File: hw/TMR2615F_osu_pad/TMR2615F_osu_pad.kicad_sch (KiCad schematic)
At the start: 78 parts, among them J1 TYPE-C-31-M-12, J10 Conn_01x04, J2 TYPE-C-31-M-12, J3 Conn_01x02, J4 TYPE-C-31-M-12, J5 XY-SH1_0-4A61, J7 Conn_01x10, J8 Conn_01x06, J9 Conn_01x23, SW1 SKSGPAE010, SW2 SKSGPAE010, U1 CA-IS3722CHS, U2 SRV05-4A, U28 SRV05-4A, U3 TMUX1574RSVR, U4 LM66100DCK, U5 AP22653W6-7, U6 SRV05-4A, U7 AT32F405RBT7-7, U8 XC6206P332MR, U9 TPS7A4700, X1 X322512MSB4SI

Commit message: Update TMR2615F_osu_pad layout/schematic, bump library submodule, add ERC report
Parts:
- removed NT1: NetTie_2, NetTie:NetTie-2_SMD_Pad2.0mm, symbol Device:NetTie_2
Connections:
- net GNDA is gone; now on net GND: C26.2, C27.1, C31.1, C32.1, C33.1, C5.1, J8.1 (Pin_1), R10.2, U3.6 (GND), U7.12 (VSSA), U9.11 (0P2V), U9.12 (0P1V), U9.17 (NC), U9.18 (NC), U9.19 (NC), U9.2 (NC), U9.21 (TP), U9.7 (GND), U9.8 (1P6V)
- net +3.3V: now also R7.2
- net +5V: now also U5.3 (EN/EN#)
- net IO9: now also R7.1, U5.4 (FAULT#); no longer U5.3 (EN/EN#)
- net VBUS_B: no longer R7.2

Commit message: before foob
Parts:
- removed C1, C4, C5: CL05B104KB54PNC, Capacitor_SMD:C_0402_1005Metric, symbol Basic_Capacitors_Resistors__C:CL05B104KB54PNC
- removed C11, C12, C13, C14, C16, C17: CL21A226MAQNNNE, Capacitor_SMD:C_0805_2012Metric, symbol Basic_Capacitors_Resistors__C:CL21A226MAQNNNE
- removed J3: Conn_01x02, Connector_PinHeader_2.54mm:PinHeader_1x02_P2.54mm_Horizontal, symbol Connector_Generic:Conn_01x02
- removed R13, R14, R15, R16: 0402WGF0000TCE, Resistor_SMD:R_0402_1005Metric, symbol Basic_Capacitors_Resistors__C:0402WGF0000TCE
- removed R7: 0402WGF1002TCE, Resistor_SMD:R_0402_1005Metric, symbol Basic_Capacitors_Resistors__C:0402WGF1002TCE
- removed R8: 0402WGF3301TCE, Resistor_SMD:R_0402_1005Metric, symbol Basic_Capacitors_Resistors__C:0402WGF3301TCE
- removed U1: CA-IS3722CHS, Isolator__C:SOIC-8_L4.9-W3.9-P1.27-LS6.0-BL, symbol Isolator__C:CA-IS3722CHS
- added C1, C2, C3, C4, C5, C6: CL21A226MAQNNNE, Capacitor_SMD:C_0805_2012Metric, symbol Basic_Capacitors_Resistors__C:CL21A226MAQNNNE
- added C10: CL10B473KB8NNNC, Capacitor_SMD:C_0603_1608Metric, symbol Basic_Capacitors_Resistors__C:CL10B473KB8NNNC
- added C12: CL21A106KAYNNNE, Capacitor_SMD:C_0805_2012Metric, symbol Basic_Capacitors_Resistors__C:CL21A106KAYNNNE
- added C28, C29: CL05B104KB54PNC, Capacitor_SMD:C_0402_1005Metric, symbol Basic_Capacitors_Resistors__C:CL05B104KB54PNC
- added D1: 1N4148WS_T4, Diode_SMD:D_SOD-323_HandSoldering, symbol Diode__C:1N4148WS_T4
- added FID1, FID2, FID3: Fiducial, Fiducial:Fiducial_1mm_Mask2mm, symbol Mechanical:Fiducial
- added H1, H2, H3: MountingHole_Pad, MountingHole:MountingHole_2.2mm_M2_Pad_Via, symbol Mechanical:MountingHole_Pad
- added R1, R10, R2, R26, R4, R6, R9: 0402WGF1002TCE, Resistor_SMD:R_0402_1005Metric, symbol Basic_Capacitors_Resistors__C:0402WGF1002TCE
- added R12, R13: 0402WGF5101TCE, Resistor_SMD:R_0402_1005Metric, symbol Basic_Capacitors_Resistors__C:0402WGF5101TCE
- added R14, R27, R3, R7: 0402WGF1200TCE, Resistor_SMD:R_0402_1005Metric, symbol Basic_Capacitors_Resistors__C:0402WGF1200TCE
- added R8: 0402WGF3300TCE, Resistor_SMD:R_0402_1005Metric, symbol Basic_Capacitors_Resistors__C:0402WGF3300TCE
- added TP1, TP10, TP11, TP12, TP13, TP14, TP15, TP16, TP2, TP3, TP4, TP5, TP6, TP7, TP8, TP9: TestPoint, TestPoint:TestPoint_Pad_D1.0mm, symbol Connector:TestPoint
- added U1: SRV05-4A, Diode__C:SOT-23-6, symbol Diode__C:SRV05-4
- added U12: SK6812MINI-E, LED__C:LED-SMD_4P-L3.2-W2.8-LS5.9_SK6812MINI-E, symbol LED__C:SK6812MINI-E_C5149201
- added U7: LM66100DCK, Package_TO_SOT_SMD:SOT-363_SC-70-6, symbol Power_Management:LM66100DCK
- R17: renamed from R4; now fitted
- R18: renamed from R5; now fitted
- renumbered C10 to C11, C31 to C13, C32 to C14, C8 to C15, C9 to C16, C2 to C17, C3 to C18, C18 to C19, C19 to C20, C20 to C21, C26 to C22, C27 to C23, C21 to C24, C22 to C25, C23 to C26, C24 to C27, C15 to C30, C25 to C31, C30 to C32, C6 to C7, C7 to C8, C33 to C9, J4 to J2, J2 to J3, J5 to J4, J7 to J5, J9 to J6, J8 to J7, J10 to J8, J6 to J9, R6 to R11, R24 to R15, R26 to R16, R1 to R19, R2 to R20, R25 to R21, R23 to R22, R10 to R23, R11 to R24, R12 to R25, R9 to R28, R3 to R5, U7 to U10, U3 to U11, U4 to U2, U5 to U3, U9 to U4, U6 to U5, U2 to U6, U28 to U9
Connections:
- net IO8 is gone; now on net IO7: J6.23 (Pin_23), U10.4 (PC15)
- net +3.3V: now also J6.4 (Pin_4), R5.2, U9.5 (VP), R1.2, R14.2, R2.2, R6.2, TP12.1, U1.5 (VP); no longer J6.3 (Pin_3)
- net +3.3VA: now also C28.2, TP3.1; no longer U11.13 (EN#)
- net +5V: now also J6.3 (Pin_3), U2.3 (~{CE}), C1.2, C2.2, C3.2, C4.2, C5.2, C6.2, D1.2 (A), TP11.1, U7.3 (~{CE}), U7.6 (VOUT); no longer C7.1, C8.2, J2.A4B9 (VBUS), J2.B4A9 (VBUS), J3.A4B9 (VBUS), J3.B4A9 (VBUS), J6.2 (Pin_2), R5.2, U3.1 (IN), U3.3 (EN/EN#), U9.5 (VP)
- net ADC1_IN0: now also TP13.1
- net ADC1_IN1: now also TP14.1
- net ADC1_IN2: now also TP15.1
- net ADC1_IN3: now also TP16.1
- net BOOT: now also R26.2
- net DIN: now also U12.4 (DOUT); no longer U10.62 (PB9)
- net GND: now also J5.9 (Pin_9), J6.16 (Pin_16), J6.2 (Pin_2), U11.13 (EN#), C1.1, C10.1, C12.2, C2.1, C28.1, C29.1, C3.1, C4.1, C5.1, C6.1, H1.1, H2.1, H3.1, R10.1, R12.1, R13.1, R26.1, R9.1, TP9.1, U1.2 (VN), U12.1 (GND), U7.2 (GND), U7.5 (ST); no longer J6.15 (Pin_15), U2.3 (~{CE})
- net I2C1_SCL: now also U9.3 (IO2), U9.4 (IO3); no longer U9.1 (IO1), U9.6 (IO4)
- net I2C1_SDA: now also U9.1 (IO1), U9.6 (IO4); no longer U9.3 (IO2), U9.4 (IO3)
- net I2C2_SCL: now also J6.11 (Pin_11); no longer J6.10 (Pin_10)
- net I2C2_SDA: now also J6.10 (Pin_10); no longer J6.9 (Pin_9)
- net IO1: now also J6.17 (Pin_17); no longer J6.16 (Pin_16)
- net IO2: now also J6.18 (Pin_18); no longer J6.17 (Pin_17)
- net IO3: now also J6.19 (Pin_19); no longer J6.18 (Pin_18)
- net IO4: now also J6.20 (Pin_20); no longer J6.19 (Pin_19)
- net IO5: now also J6.21 (Pin_21); no longer J6.20 (Pin_20)
- net IO6: now also J6.22 (Pin_22), U10.3 (PC14); no longer J6.21 (Pin_21), U10.2 (PC13)
- net IO7: no longer J6.22 (Pin_22), U10.3 (PC14)
- net SPI3_CS: now also J6.12 (Pin_12); no longer J6.11 (Pin_11)
- net SPI3_MISO: now also J6.14 (Pin_14); no longer J6.13 (Pin_13)
- net SPI3_MOSI: now also J6.15 (Pin_15); no longer J6.14 (Pin_14)
- net SPI3_SCK: now also J6.13 (Pin_13); no longer J6.12 (Pin_12)
- net TMUX_S4A: now also R8.1, TP6.1; no longer J5.10 (Pin_10)
- net TMUX_S4B: now also J5.10 (Pin_10); no longer J5.9 (Pin_9)
- net UART7_RX: now also U10.37 (PC6), R2.1, R3.2, U1.1 (IO1), U1.6 (IO4)
- net UART7_TX: now also U10.38 (PC7), R1.1, R7.2, U1.3 (IO2), U1.4 (IO3)
- net UART8_RX: now also J6.6 (Pin_6); no longer J6.5 (Pin_5)
- net UART8_TX: now also J6.5 (Pin_5); no longer J6.4 (Pin_4)
- net USART1_CK: now also J6.9 (Pin_9); no longer J6.8 (Pin_8)
- net USART1_RX: now also J6.7 (Pin_7); no longer J6.6 (Pin_6)
- net USART1_TX: now also J6.8 (Pin_8); no longer J6.7 (Pin_7)
- net VBUS_B: now also C12.1, R4.2, TP4.1
- net at J1.A6 (DP1), J1.B6 (DP2): now also R7.1, TP1.1
- net at J1.A7 (DN1), J1.B7 (DN2): now also R3.1, TP2.1
- net at J1.A5 (CC1): now also R13.2
- net at J1.B5 (CC2): now also R12.2
- net at R15.2, R22.2: now also R14.1
- net IO10 renamed LM_ST
- net LM_ST: now also TP5.1
- net IO9 renamed AP_FAULT
- net AP_FAULT: now also R6.1, TP7.1
- new net: C10.2, R4.1, R8.2, R9.2
- new net: R27.1, U12.2 (DIN)
- new net: R27.2, U10.62 (PB9)
- new net: C29.2, D1.1 (K), U12.3 (VDD)
- new net PW_PSTRH: R10.2, TP8.1, U10.2 (PC13), U3.3 (EN/EN#)
- new net VBUS_HOST: C7.1, C8.2, J3.A4B9 (VBUS), J3.B4A9 (VBUS), TP10.1, U3.1 (IN), U7.1 (VIN)
- no-connect marks 6 -> 14
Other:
- note removed: "For End User Installation"
- moved on the sheet: C11, C15, C16, C17, C18, C19, C20, C21, C22, C23, C24, C25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

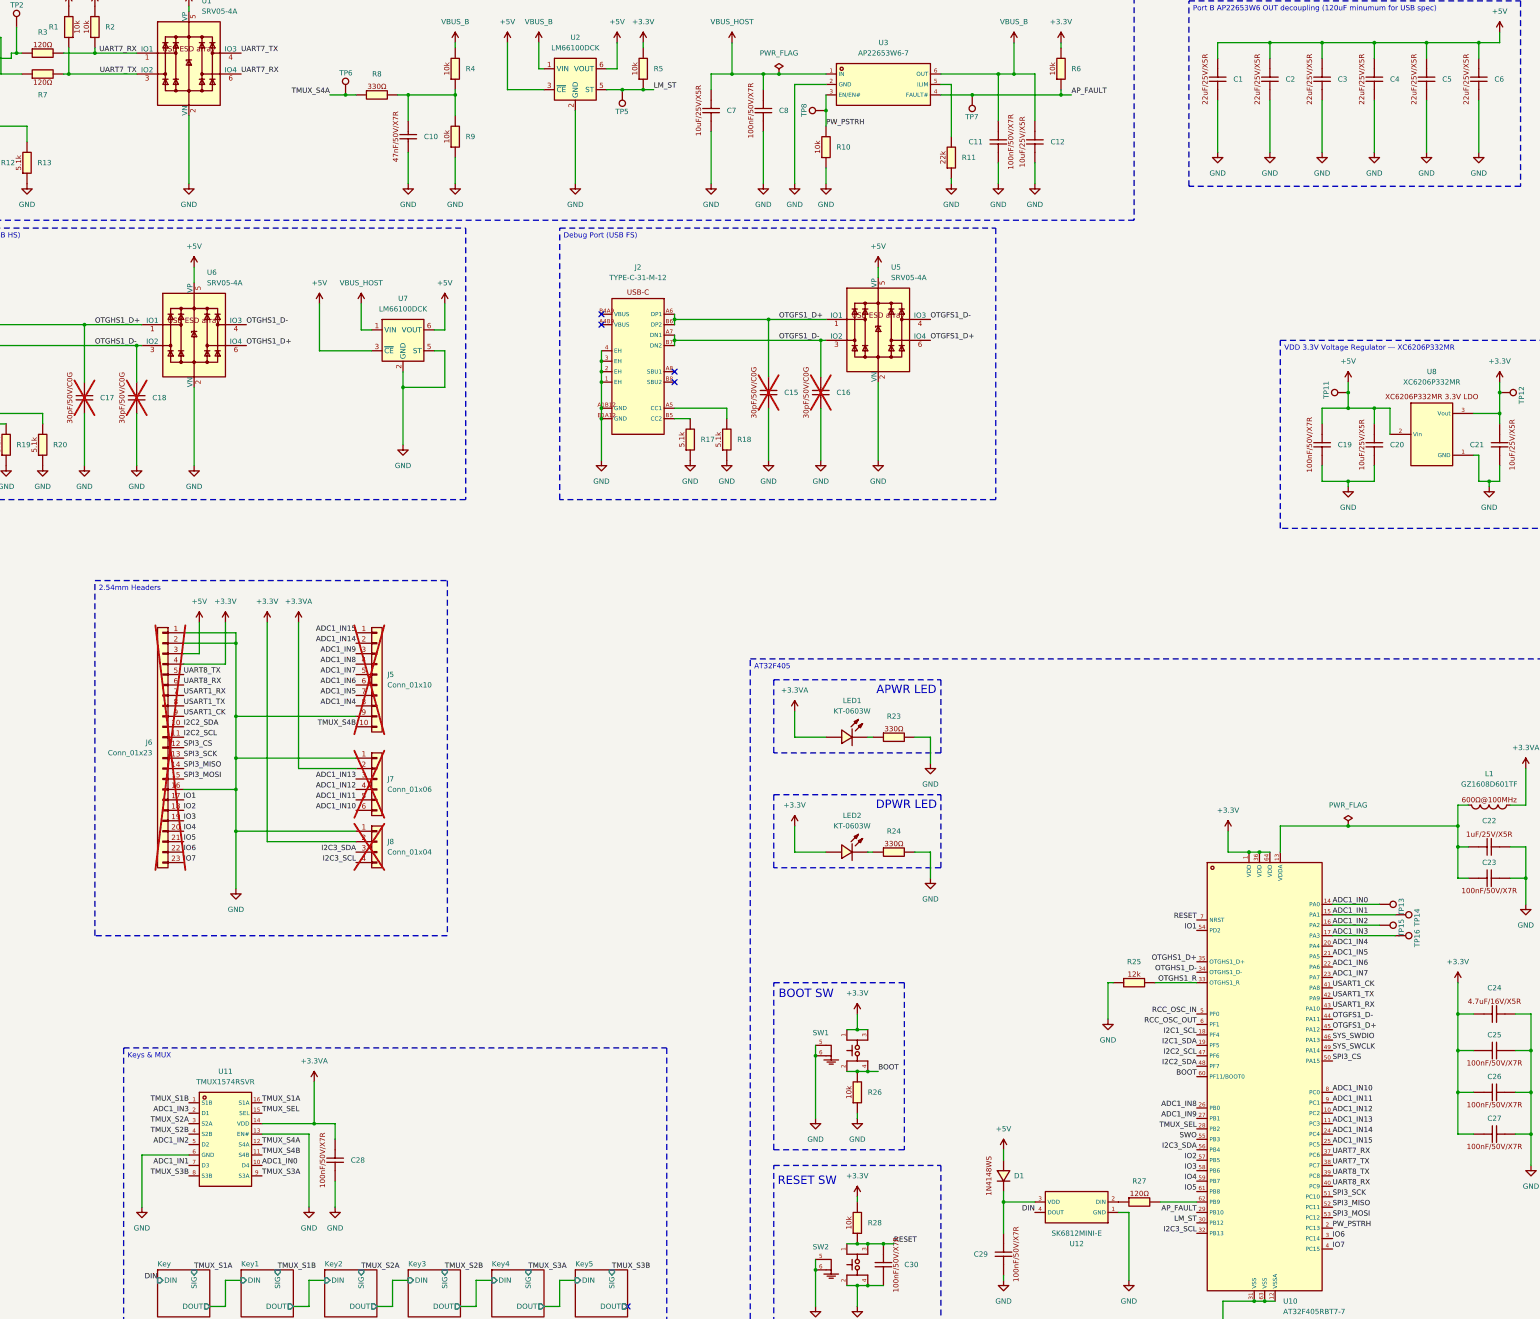
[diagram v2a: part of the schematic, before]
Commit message: Clear the pre-fab blockers on TMR2615F_osu_pad
All three blockers from prefab_review_2026-08-03.md, plus the should-fix
resistor and a filter retune, in schematic and layout.

U8 XC6206P332MR pinout corrected to the SOT-23 assignment in the LCSC
datasheet — 1=VSS, 2=VOUT, 3=VIN. Pad 2 now carries +3.3V and pad 3 +5V;
before this the +3.3V rail would have come up at ~4.4 V through the pass
device's body diode, past the AT32F405's 4.0 V absolute maximum.

I2C1 SDA and SCL swapped at the MCU so PF4=SDA and PF5=SCL, matching
AT32F405 datasheet Table 9. These pins have no internal remap, so J4's
accessory port had no working hardware I2C before.

U6 (SRV05-4A, SOT-23-6, 3-5 pF per channel and doubled onto each line)
deleted from the USB HS pair and replaced with U25/U26, one
PESD5V0R1BSFYL each on D+ and D-: SOD-962, 0.15 pF, which fits the
~1-2 pF budget at 480 Mbps. The pair was re-dressed around the new
footprints (1789 -> 1766 segments, 628 -> 620 vias). A schematic note
records the fallback: the 0201-class parts can be omitted, or 0402
sub-3 pF diodes fitted on the DNP C17/C18 pads, if assembly balks.

BOOT0 pull-down R26 10 k -> 3.3 k. Table 9 footnote 7 asks for 3.3 kohm
or below.

Sensor and VBUS_B sense filters retuned from 330 ohm + 47 nF to
5.1 kohm + 3.3 nF (R8, R29-R34; C10, C34, C38, C42, C46, C50, C54).
47 nF was over the TMR2615's 10 nF maximum load capacitance; 3.3 nF is
inside it, and the larger series resistor keeps the corner where it was
(tau 16.8 us, f_c 9.46 kHz).

LCSC codes filled in for the three parts the fab BOM could not source
automatically: U2/U7 LM66100DCK = C2869734, U4 TPS7A4700 = C28286.
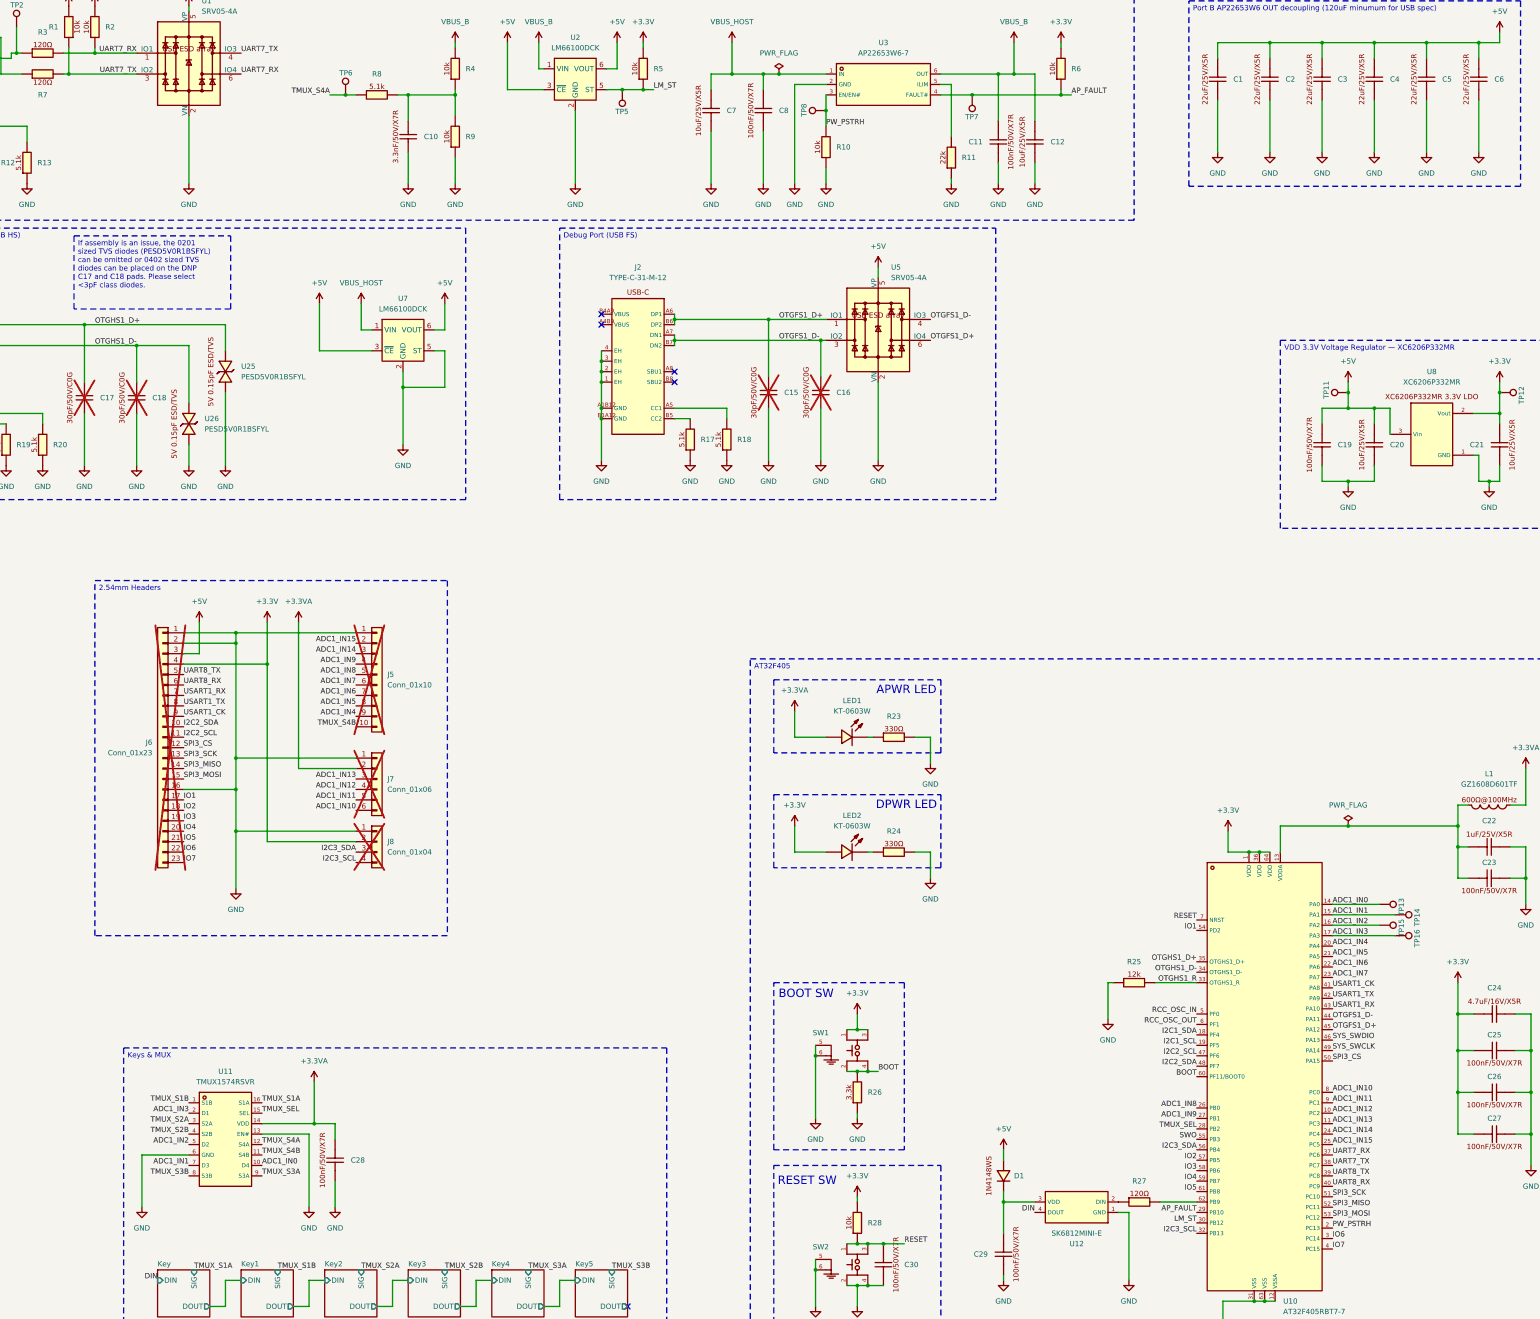
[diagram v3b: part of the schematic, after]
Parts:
- removed R26: 0402WGF1002TCE, Resistor_SMD:R_0402_1005Metric, symbol Basic_Capacitors_Resistors__C:0402WGF1002TCE
- removed U6: SRV05-4A, Diode__C:SOT-23-6, symbol Diode__C:SRV05-4
- added R26: 0402WGF3301TCE, Resistor_SMD:R_0402_1005Metric, symbol Basic_Capacitors_Resistors__C:0402WGF3301TCE
- added U25, U26: PESD5V0R1BSFYL, Diode__C:SOD-962_L0.6-W0.3-BI, symbol Diode__C:PESD5V0R1BSFYL
- C10: value CL10B473KB8NNNC -> CL10B332KB8NNNC; symbol Basic_Capacitors_Resistors__C:CL10B473KB8NNNC -> Basic_Capacitors_Resistors__C:CL10B332KB8NNNC; LCSC C1622 -> C1613; Symbol Name CL10B473KB8NNNC -> CL10B332KB8NNNC
- R8: value 0402WGF3300TCE -> 0402WGF5101TCE; symbol Basic_Capacitors_Resistors__C:0402WGF3300TCE -> Basic_Capacitors_Resistors__C:0402WGF5101TCE; LCSC C25104 -> C25905; Symbol Name 0402WGF3300TCE -> 0402WGF5101TCE
- U2, U7: LCSC (none) -> C2869734
- U4: LCSC (none) -> C28286
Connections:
- net +3.3V: now also U8.2 (Vout); no longer U8.3 (Vout)
- net +5V: now also U8.3 (Vin); no longer U8.2 (Vin)
- net ADC1_IN14: now also J5.3 (Pin_3); no longer J5.2 (Pin_2)
- net ADC1_IN15: now also J5.2 (Pin_2); no longer J5.1 (Pin_1)
- net ADC1_IN4: now also J5.9 (Pin_9); no longer J5.8 (Pin_8)
- net ADC1_IN5: now also J5.8 (Pin_8); no longer J5.7 (Pin_7)
- net ADC1_IN6: now also J5.7 (Pin_7); no longer J5.6 (Pin_6)
- net ADC1_IN7: now also J5.6 (Pin_6); no longer J5.5 (Pin_5)
- net ADC1_IN8: now also J5.5 (Pin_5); no longer J5.4 (Pin_4)
- net ADC1_IN9: now also J5.4 (Pin_4); no longer J5.3 (Pin_3)
- net BOOT: now also R26.2
- net GND: now also J5.1 (Pin_1), R26.1, U25.1, U26.1; no longer J5.9 (Pin_9)
- net I2C1_SCL: now also U10.19 (PF5); no longer U10.18 (PF4)
- net I2C1_SDA: now also U10.18 (PF4); no longer U10.19 (PF5)
- net OTGHS1_D+: now also U25.2
- net OTGHS1_D-: now also U26.2
